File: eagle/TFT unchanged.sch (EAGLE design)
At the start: 22 parts, among them IC5 APX803, P3 TPB1,27, P5V TPB1,27, Q1 MMBT2222, U2 MIC5225-3.3, U3 74HC4050D

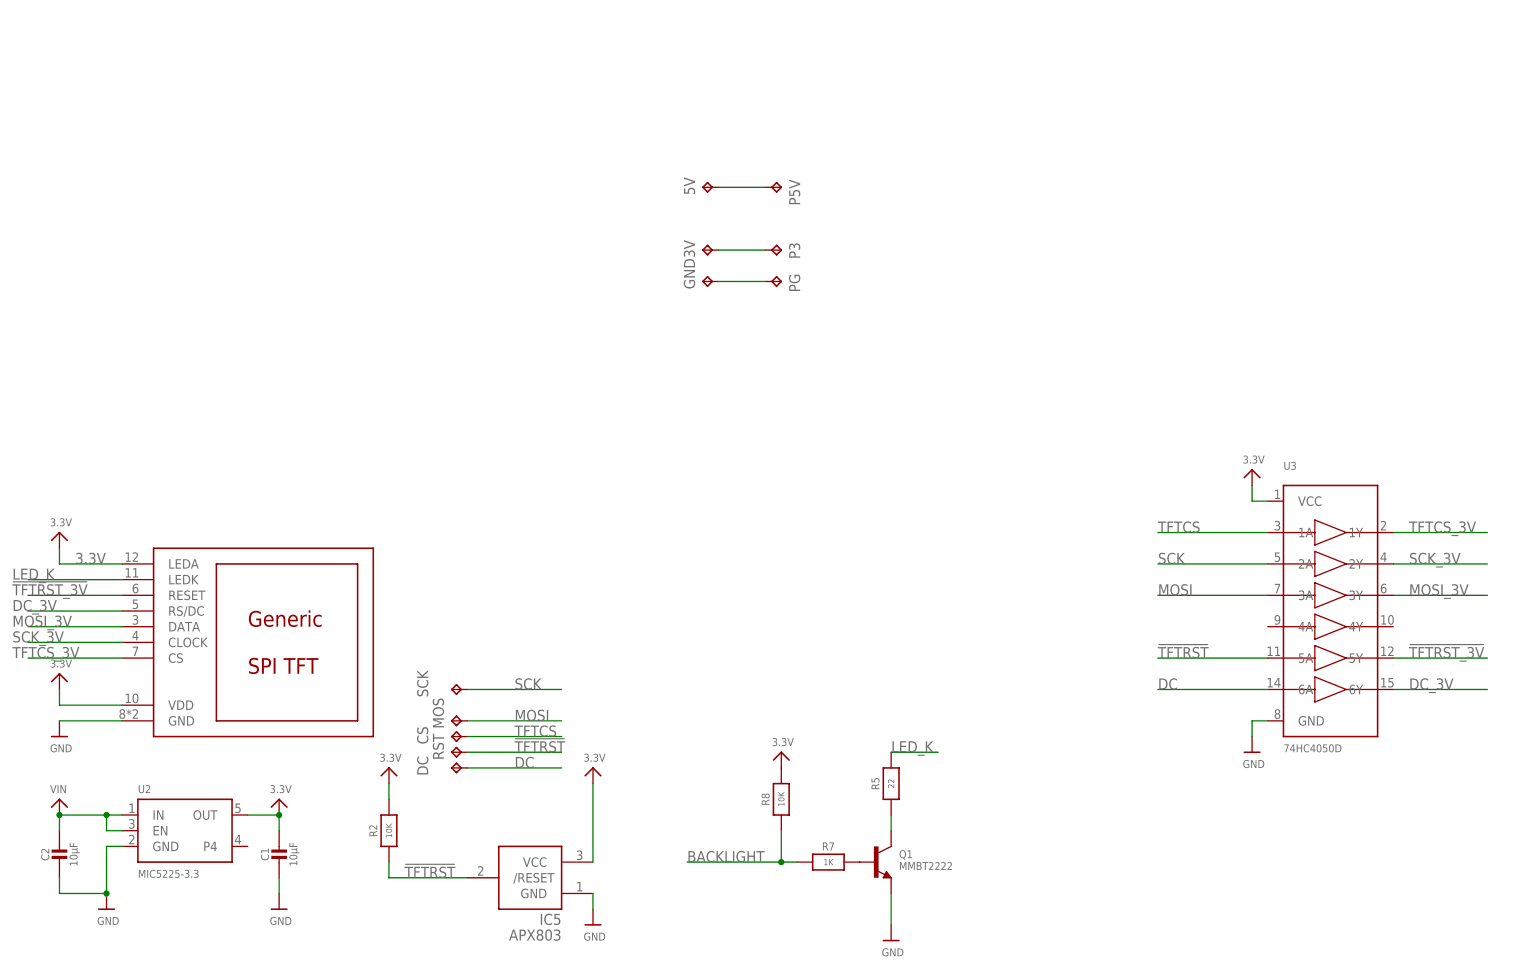
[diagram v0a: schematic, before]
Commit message: Added source TFT eagle files
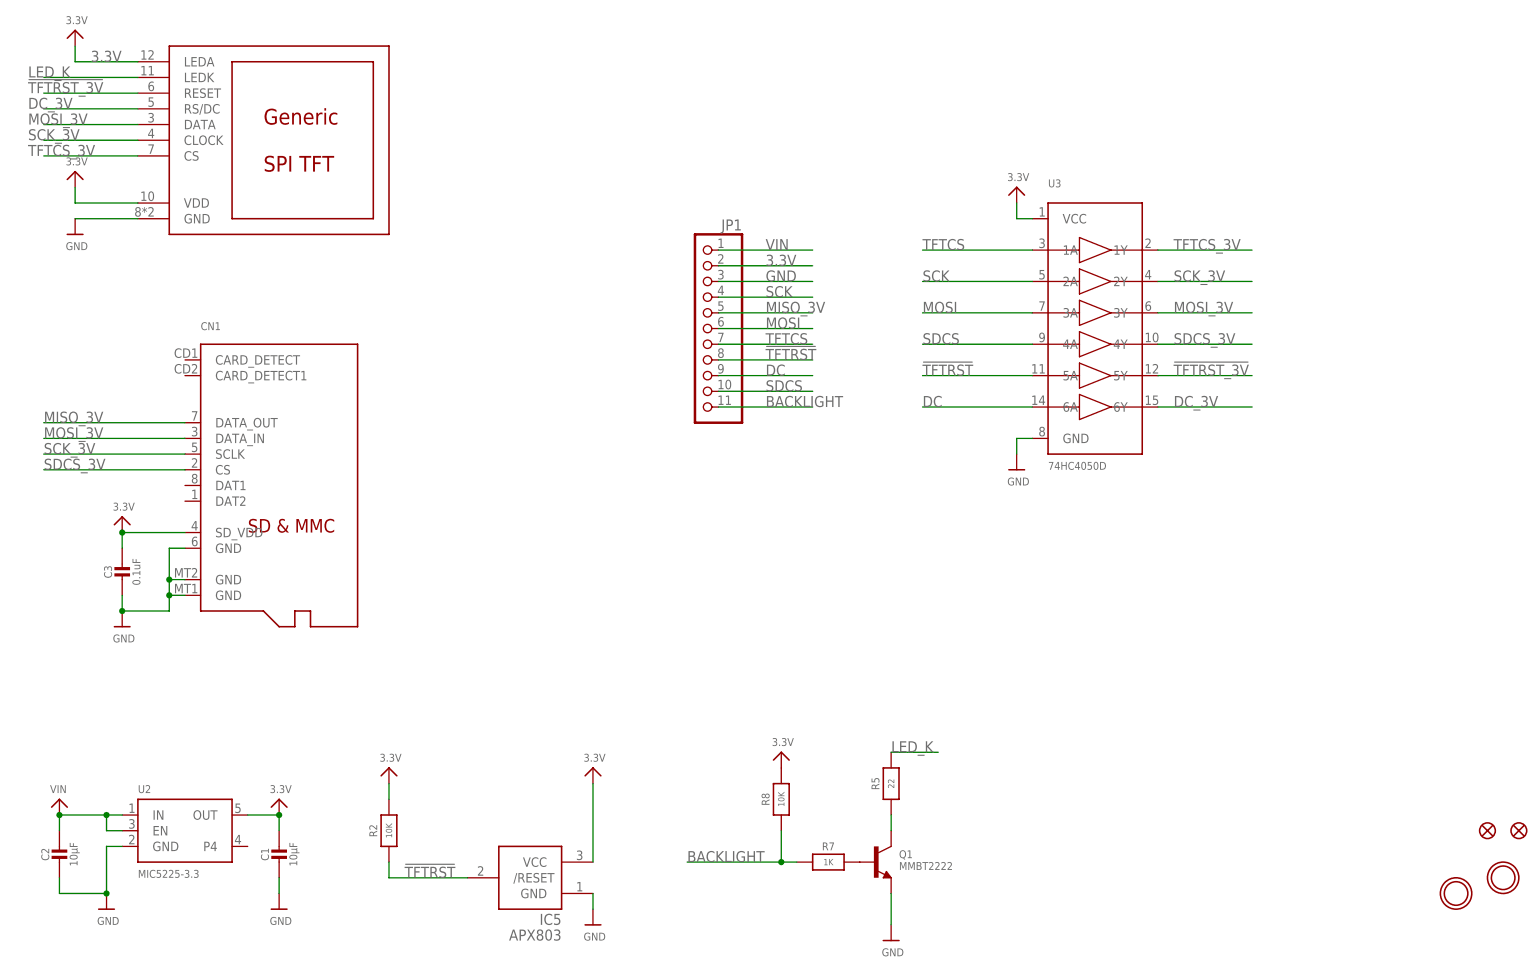
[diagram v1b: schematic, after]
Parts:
- removed 3V, 5V, CS, DC, GND, MOS, P3, P5V, PG, RST, SCK: TPB1,27, testpad:TPB1,27
- added C3: 0.1uF, microbuilder:CAP_CERAMIC0805-NOOUTLINE
- added CN1: (no value), microbuilder:MICROSD
- added FID1, FID2: FIDUCIAL_1MM, microbuilder:FIDUCIAL_1MM
- added JP1: (no value), microbuilder:HEADER-1X11
- added U$10, U$9: MOUNTINGHOLE2.5, microbuilder:MOUNTINGHOLE2.5
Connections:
- removed net N$2: 5V.TP, P5V.TP
- new net MISO_3V: CN1.DATA_OUT, JP1.5
- new net SDCS: JP1.10, U3.4A
- new net SDCS_3V: CN1.CS, U3.4Y
- net !TFTRST: now also JP1.8; no longer RST.TP
- net 3.3V: now also C3.1, CN1.SD_VDD, JP1.2
- net BACKLIGHT: now also JP1.11
- net DC: now also JP1.9; no longer DC.TP
- net GND: now also C3.2, CN1.GND@1, CN1.GND@2, CN1.GND@3, JP1.3; no longer GND.TP, PG.TP
- net MOSI: now also JP1.6; no longer MOS.TP
- net MOSI_3V: now also CN1.DATA_IN
- net SCK: now also JP1.4; no longer SCK.TP
- net SCK_3V: now also CN1.SCLK
- net TFTCS: now also JP1.7; no longer CS.TP
- net VIN: now also JP1.1; no longer 3V.TP, P3.TP
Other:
- moved on the sheet: U3
